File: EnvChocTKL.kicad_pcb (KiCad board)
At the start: 2 copper layers, 343.3 x 115.1 mm, 181 parts, among them U1 EliteC

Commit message: DERP! - missing trace, D12 to pin2 of Switch 12
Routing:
- net Net-(D_12-Pad2): track 0.00 -> 5.62 mm

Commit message: fixed issues with footprint and required board changes + updated gerber
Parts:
- K_0, K_1, K_10, K_11, K_12, K_13, K_14, K_15, K_16, K_17, K_18, K_19, K_2, K_20, K_21, K_22, K_23, K_24, K_25, K_26, K_27, K_28, K_3, K_30, K_31, K_32, K_34, K_35, K_36, K_37, K_38, K_39, K_4, K_40, K_41, K_42, K_43, K_44, K_45, K_47, K_48, K_49, K_5, K_51, K_52, K_53, K_54, K_55, K_56, K_57, K_58, K_59, K_6, K_60, K_61, K_62, K_64, K_65, K_66, K_67, K_68, K_69, K_7, K_70, K_71, K_72, K_73, K_74, K_76, K_8, K_85, K_86, K_87, K_9: footprint Switch_Keyboard_Kailh:SW_Kailh_Choc_V1_1.00u -> Switch_Keyboard_Kailh:SW_Kailh_Choc_V2
- K_29: footprint Switch_Keyboard_Kailh:SW_Kailh_Choc_V1_2.00u -> Switch_Keyboard_Kailh:SW_Kailh_Choc_V2
- K_33: footprint Switch_Keyboard_Kailh:SW_Kailh_Choc_V1_1.50u -> Switch_Keyboard_Kailh:SW_Kailh_Choc_V2
- K_46: footprint Switch_Keyboard_Kailh:SW_Kailh_Choc_V1_ISOEnter -> Switch_Keyboard_Kailh:SW_Kailh_Choc_V2
- K_50: footprint Switch_Keyboard_Kailh:SW_Kailh_Choc_V1_1.75u -> Switch_Keyboard_Kailh:SW_Kailh_Choc_V2
- K_63, K_77, K_78, K_79, K_81, K_82, K_83, K_84: footprint Switch_Keyboard_Kailh:SW_Kailh_Choc_V1_1.25u -> Switch_Keyboard_Kailh:SW_Kailh_Choc_V2
- K_75: footprint Switch_Keyboard_Kailh:SW_Kailh_Choc_V1_2.75u -> Switch_Keyboard_Kailh:SW_Kailh_Choc_V2
- K_80: footprint Switch_Keyboard_Kailh:SW_Kailh_Choc_V1_6.25u -> Switch_Keyboard_Kailh:SW_Kailh_Choc_V2
- moved D_11 3.89 mm to (255.8, 138.0)
- moved D_10 3.21 mm to (236.0, 138.2)
- moved D_9 2.93 mm to (216.6, 138.2)
- moved D_3 2.34 mm to (103.2, 138.2)
- moved D_2 2.15 mm to (84.0, 138.2)
- moved D_8 2.13 mm to (197.8, 138.2)
- moved D_7 2.13 mm to (178.8, 138.2)
- moved D_12 1.88 mm to (272.6, 138.0)
- moved D_14 1.86 mm to (310.6, 138.0)
- moved D_5 1.74 mm to (140.0, 138.2)
- moved D_6 1.66 mm to (159.6, 138.2)
- moved D_4 1.64 mm to (121.6, 138.2)
- moved D_1 1.52 mm to (64.4, 138.2)
- moved D_13 1.35 mm to (291.0, 138.0)
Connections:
- U1 pad 21: (no net) -> Net-(U1-Pad21)
- U1 pad 22: (no net) -> Net-(U1-Pad22)
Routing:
- net row0: track 319.2 -> 336.4 mm
- net row5: track 431.0 -> 437.1 mm
- net Net-(D_10-Pad2): track 5.73 -> 8.52 mm
- net Net-(D_11-Pad2): track 6.18 -> 8.76 mm
- net Net-(D_3-Pad2): track 4.94 -> 7.43 mm
- net Net-(D_7-Pad2): track 5.79 -> 8.10 mm
- net Net-(D_2-Pad2): track 5.11 -> 7.35 mm
- net Net-(D_9-Pad2): track 5.96 -> 8.00 mm
- net Net-(D_8-Pad2): track 6.11 -> 8.00 mm
- net Net-(D_1-Pad2): track 5.46 -> 7.08 mm
- net Net-(D_5-Pad2): track 5.54 -> 7.13 mm
- net Net-(D_12-Pad2): track 5.62 -> 7.15 mm
- net Net-(D_14-Pad2): track 6.23 -> 7.76 mm
- net Net-(D_13-Pad2): track 5.59 -> 6.98 mm
- net Net-(D_4-Pad2): track 5.43 -> 6.80 mm
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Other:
- board text added: "https://github.com/Envious-Data/Env-ChocV2TKL Revision 17 PROTOTYPE"
- board text removed: "https://github.com/Envious-Data/Env-ChocV2TKL Revision 16"

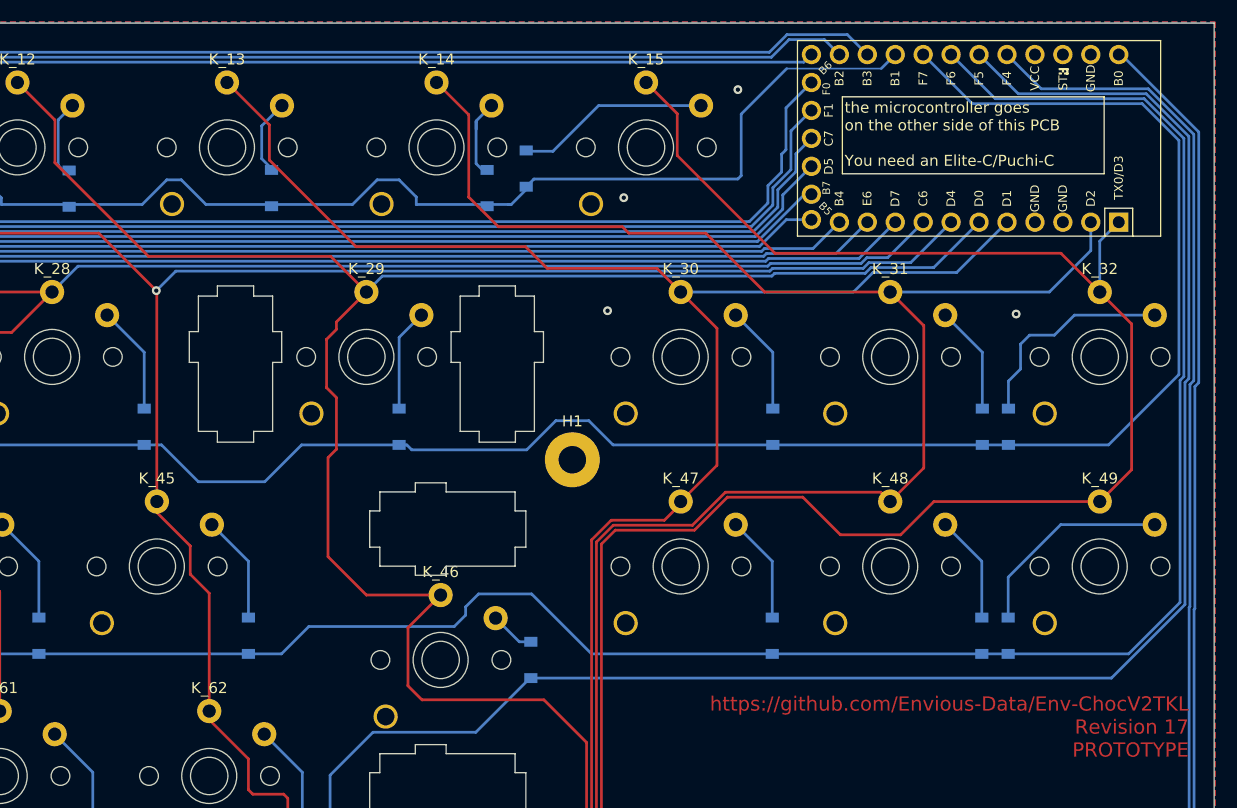
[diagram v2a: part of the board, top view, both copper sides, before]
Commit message: adjusted couple traces and sorted out revision
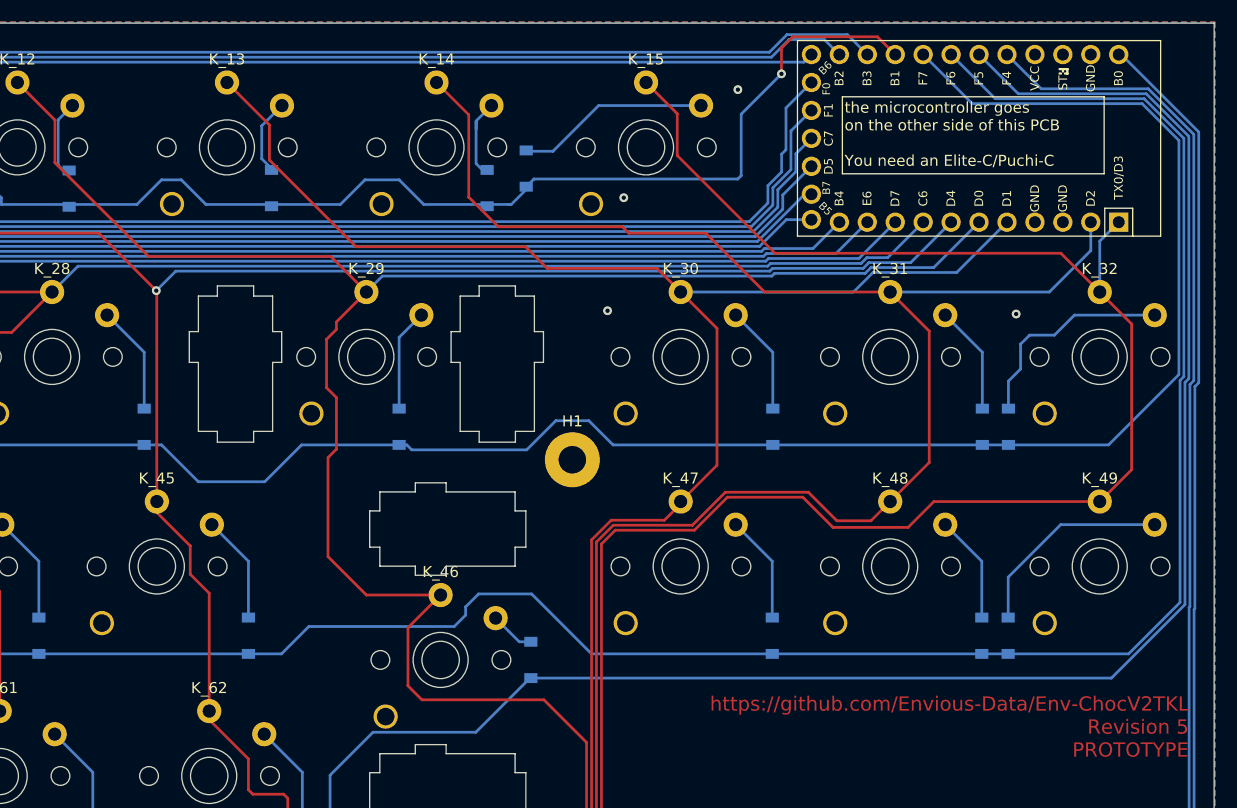
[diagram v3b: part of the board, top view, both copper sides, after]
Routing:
- net row0: track 336.4 -> 338.7 mm, vias 0 -> 1
- net col16: track 211.5 -> 213.3 mm
- net col17: track 229.2 -> 228.7 mm
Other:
- board text added: "https://github.com/Envious-Data/Env-ChocV2TKL Revision 5 PROTOTYPE"
- board text removed: "https://github.com/Envious-Data/Env-ChocV2TKL Revision 17 PROTOTYPE"
